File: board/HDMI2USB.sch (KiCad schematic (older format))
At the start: 0 parts

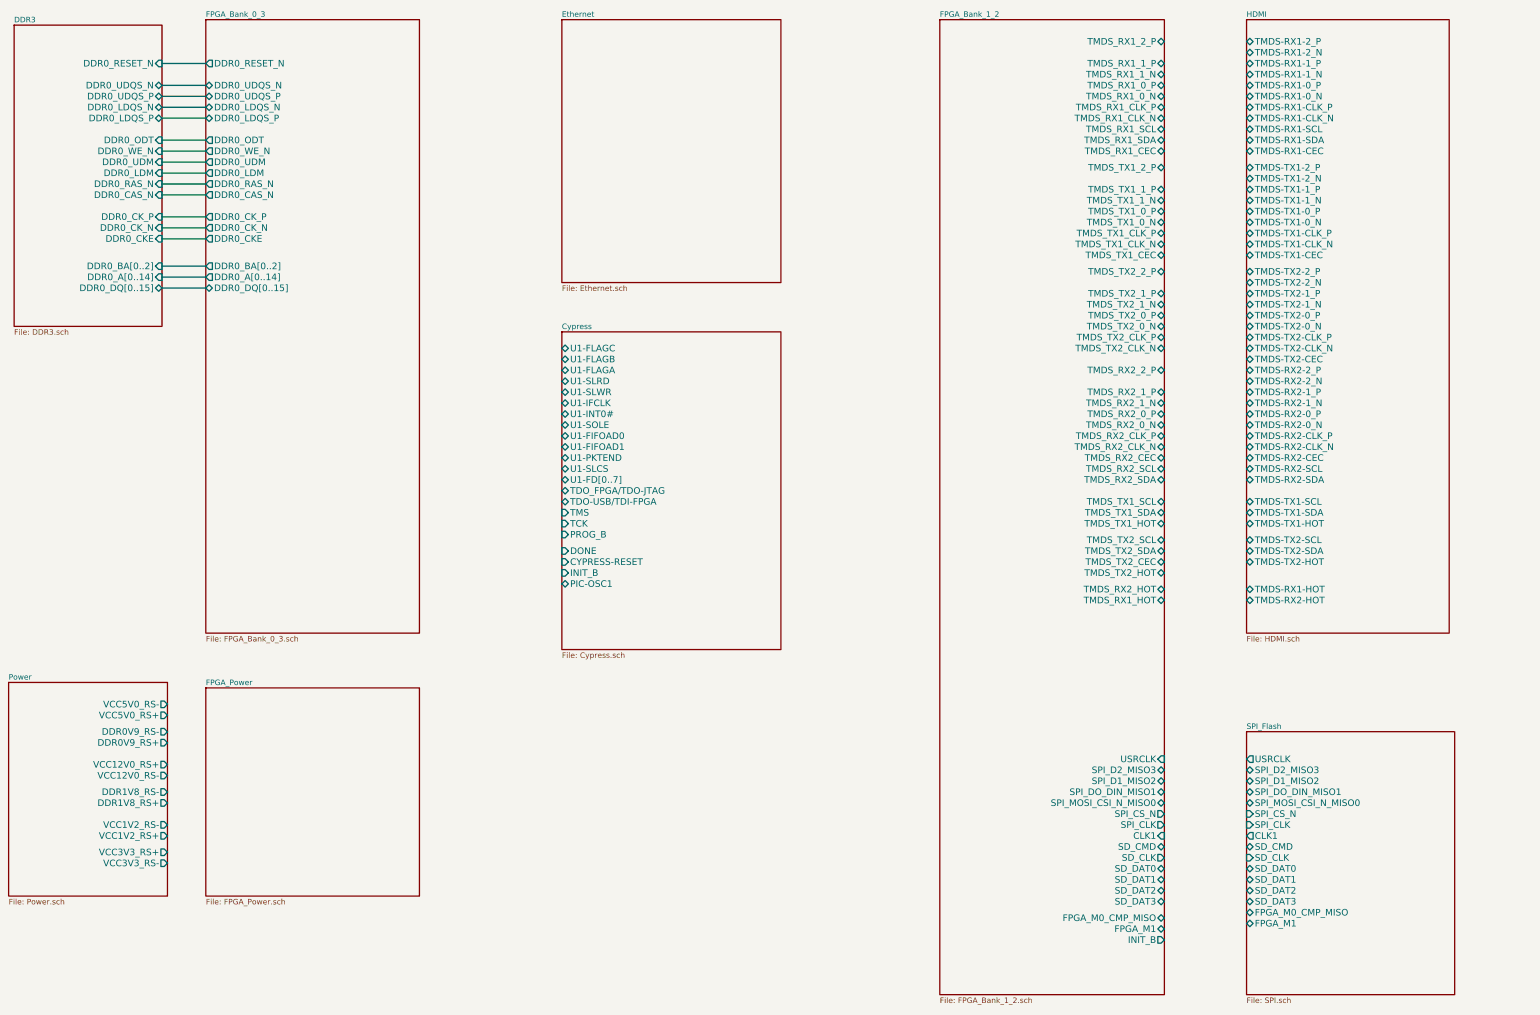
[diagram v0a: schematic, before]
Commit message: Issue #1458 - HDMI RX TX pins added, Cypress added, DDR added
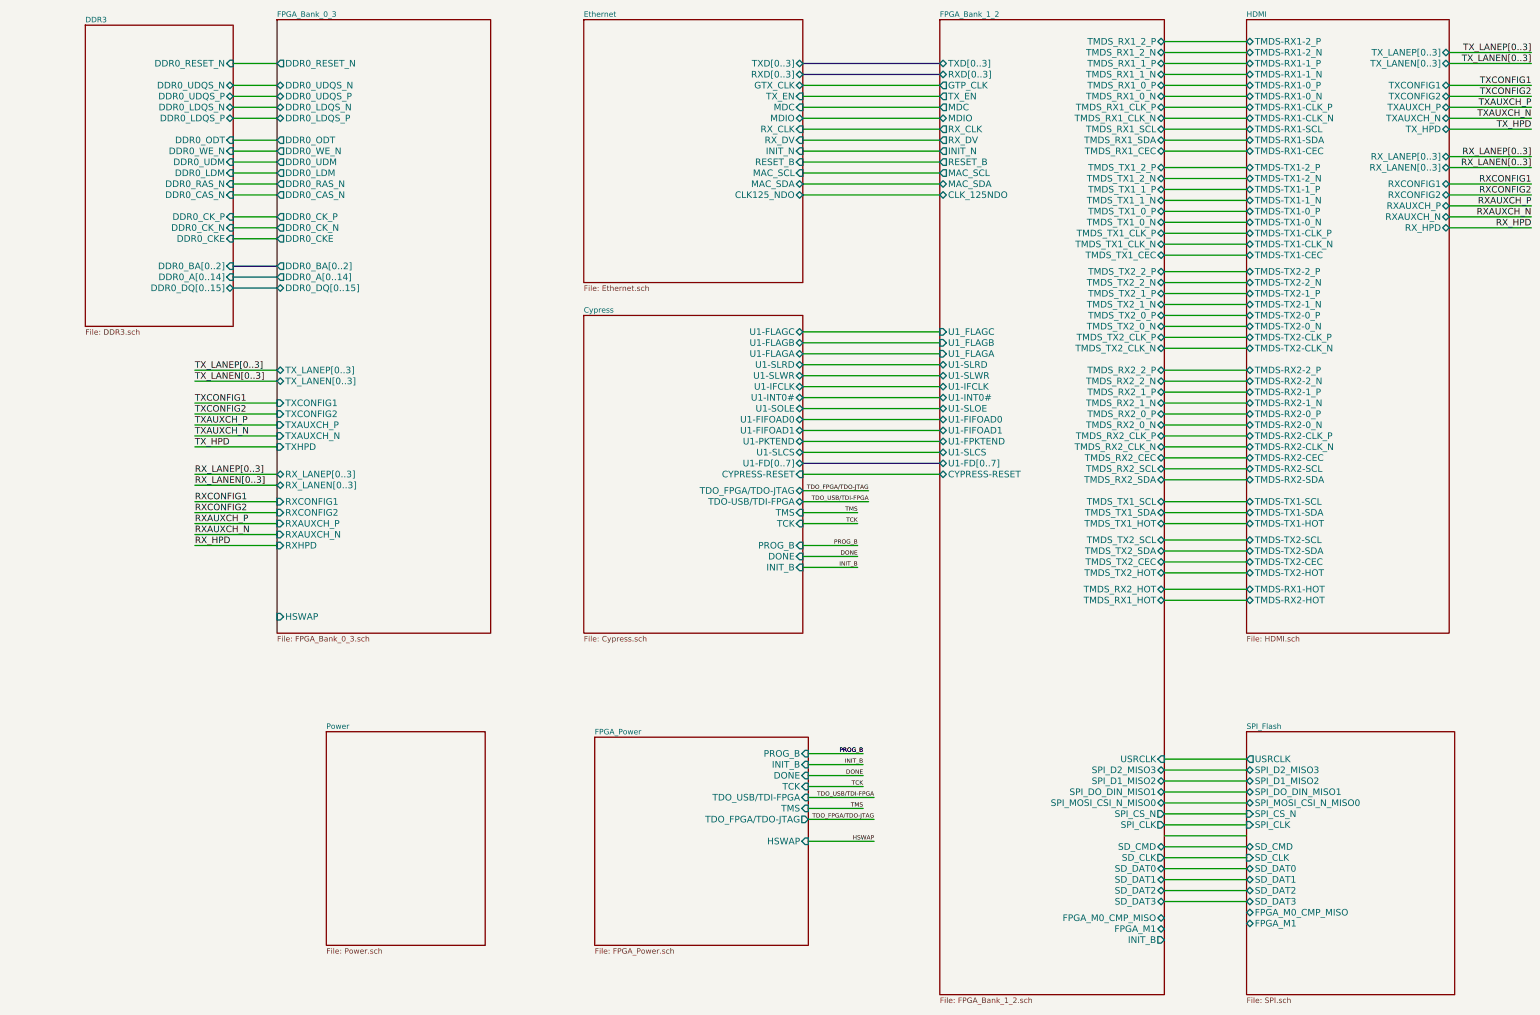
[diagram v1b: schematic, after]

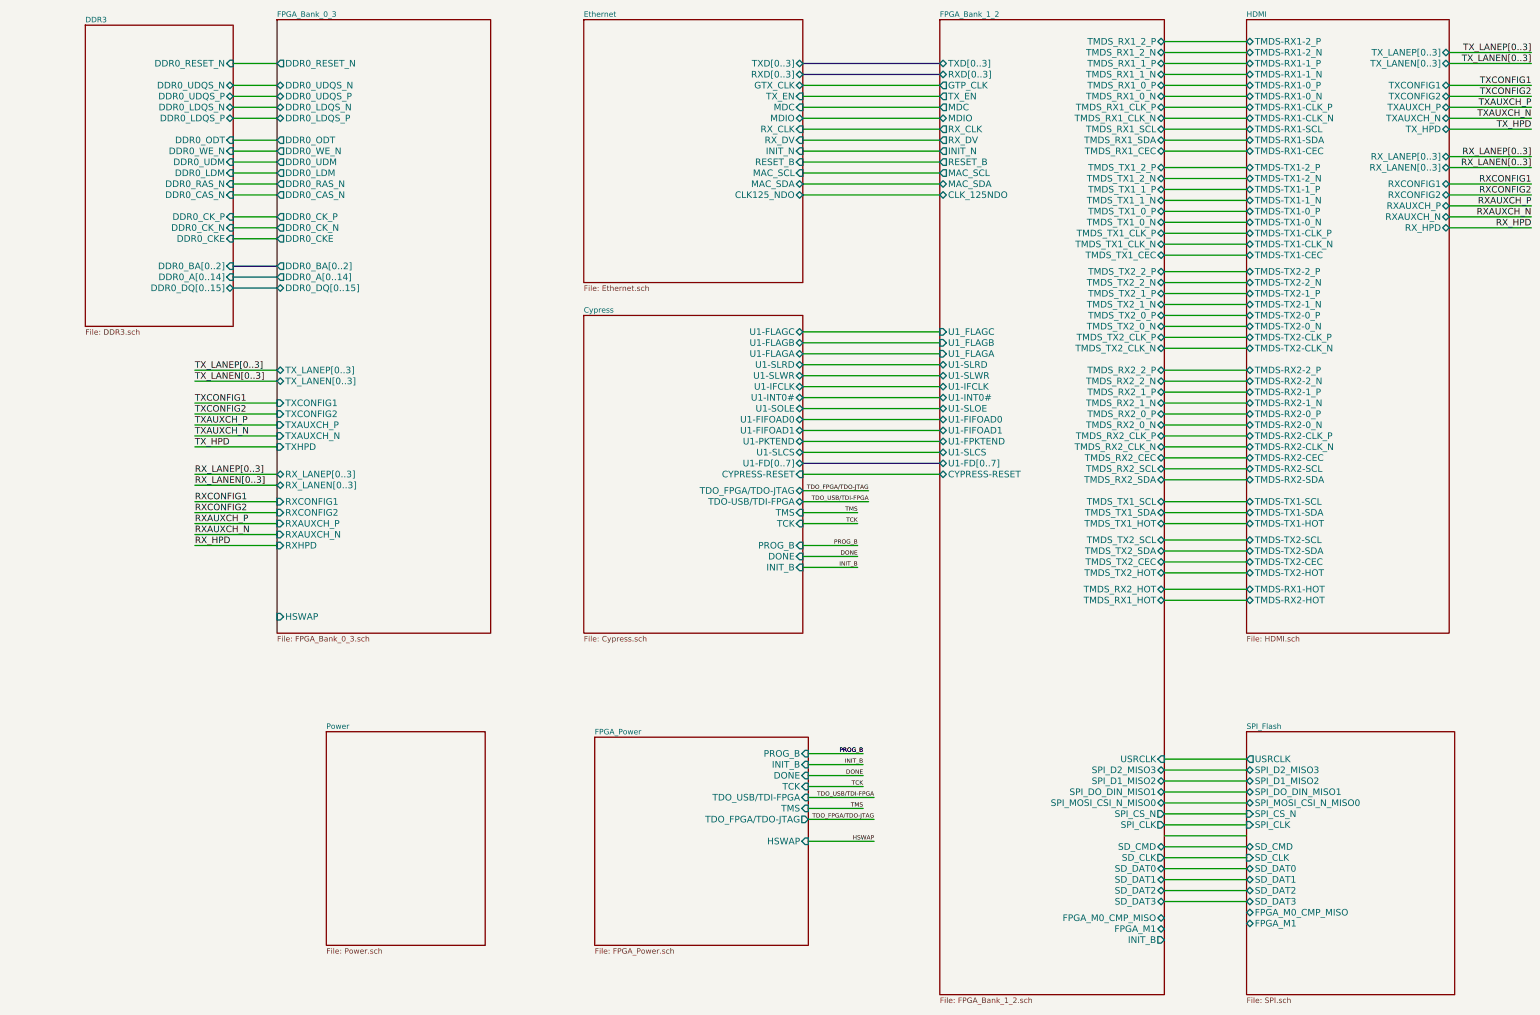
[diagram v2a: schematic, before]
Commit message: Issue #1470 - HDMI Sheet changes
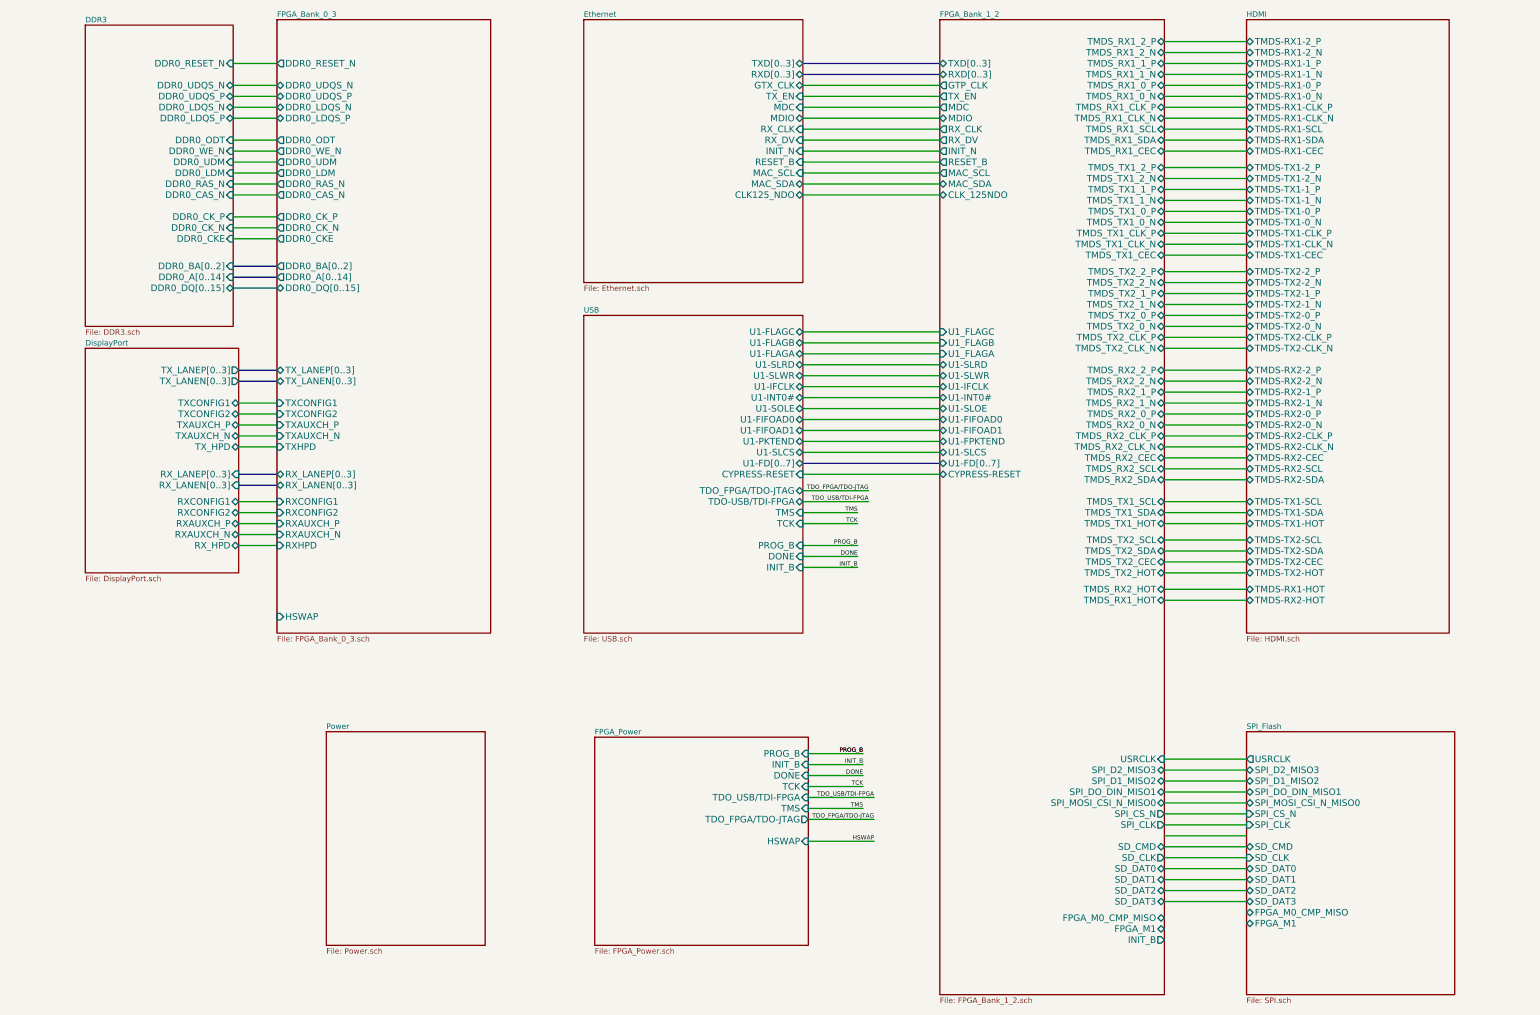
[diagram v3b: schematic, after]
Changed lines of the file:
@@
 LIBS:contrib
 LIBS:valves
-LIBS:hdmi2usb
 LIBS:HDMI2USB-cache
 EELAYER 27 0
@@
 $Descr A3 16535 11693
 encoding utf-8
-Sheet 1 10
+Sheet 1 11
 Title "HDMI2USB"
-Date "19 dec 2014"
+Date "29 dec 2014"
 Rev "Rev2"
 Comp ""
@@
 F32 "RXHPD" I L 3750 5900 60
 F33 "RXAUXCH_N" I L 3750 5800 60
-$EndSheet
-$Sheet
-S 12600 1100 1850 5600
-U 548A04AA
-F0 "HDMI" 50
-F1 "HDMI.sch" 50
-F2 "TMDS-RX1-2_P" B L 12600 1300 60
-F3 "TMDS-RX1-1_P" B L 12600 1500 60
-F4 "TMDS-RX1-0_P" B L 12600 1700 60
-F5 "TMDS-RX1-2_N" B L 12600 1400 60
-F6 "TMDS-RX1-1_N" B L 12600 1600 60
-F7 "TMDS-RX1-0_N" B L 12600 1800 60
-F8 "TMDS-RX1-CLK_P" B L 12600 1900 60
-F9 "TMDS-RX1-CLK_N" B L 12600 2000 60
-F10 "TMDS-RX1-SCL" B L 12600 2100 60
-F11 "TMDS-RX1-SDA" B L 12600 2200 60
-F12 "TMDS-TX1-2_P" B L 12600 2450 60
-F13 "TMDS-TX1-1_P" B L 12600 2650 60
-F14 "TMDS-TX1-0_P" B L 12600 2850 60
-F15 "TMDS-TX1-2_N" B L 12600 2550 60
-F16 "TMDS-TX1-1_N" B L 12600 2750 60
-F17 "TMDS-TX1-0_N" B L 12600 2950 60
-F18 "TMDS-TX1-CLK_P" B L 12600 3050 60
-F19 "TMDS-TX1-CLK_N" B L 12600 3150 60
-F20 "TMDS-TX2-2_P" B L 12600 3400 60
-F21 "TMDS-TX2-1_P" B L 12600 3600 60
-F22 "TMDS-TX2-0_P" B L 12600 3800 60
-F23 "TMDS-TX2-2_N" B L 12600 3500 60
-F24 "TMDS-TX2-1_N" B L 12600 3700 60
-F25 "TMDS-TX2-0_N" B L 12600 3900 60
-F26 "TMDS-TX2-CLK_P" B L 12600 4000 60
-F27 "TMDS-TX2-CLK_N" B L 12600 4100 60
-F28 "TMDS-RX2-2_P" B L 12600 4300 60
-F29 "TMDS-RX2-1_P" B L 12600 4500 60
-F30 "TMDS-RX2-0_P" B L 12600 4700 60
-F31 "TMDS-RX2-2_N" B L 12600 4400 60
-F32 "TMDS-RX2-1_N" B L 12600 4600 60
-F33 "TMDS-RX2-0_N" B L 12600 4800 60
-F34 "TMDS-RX2-CLK_P" B L 12600 4900 60
-F35 "TMDS-RX2-CLK_N" B L 12600 5000 60
-F36 "TMDS-TX1-CEC" B L 12600 3250 60
-F37 "TMDS-TX2-CEC" B L 12600 6050 60
-F38 "TMDS-RX1-CEC" B L 12600 2300 60
-F39 "TMDS-RX2-CEC" B L 12600 5100 60
-F40 "TMDS-RX2-SCL" B L 12600 5200 60
-F41 "TMDS-RX2-SDA" B L 12600 5300 60
-F42 "TMDS-TX1-SCL" B L 12600 5500 60
-F43 "TMDS-TX1-SDA" B L 12600 5600 60
-F44 "TMDS-TX1-HOT" B L 12600 5700 60
-F45 "TMDS-TX2-SCL" B L 12600 5850 60
-F46 "TMDS-TX2-SDA" B L 12600 5950 60
-F47 "TMDS-TX2-HOT" B L 12600 6150 60
-F48 "TMDS-RX1-HOT" B L 12600 6300 60
-F49 "TMDS-RX2-HOT" B L 12600 6400 60
-F50 "TX_LANEP[0..3]" B R 14450 1400 60
-F51 "TXCONFIG1" B R 14450 1700 60
-F52 "TXCONFIG2" B R 14450 1800 60
-F53 "TXAUXCH_P" B R 14450 1900 60
-F54 "TXAUXCH_N" B R 14450 2000 60
-F55 "RXCONFIG1" B R 14450 2600 60
-F56 "RXCONFIG2" B R 14450 2700 60
-F57 "RXAUXCH_P" B R 14450 2800 60
-F58 "RXAUXCH_N" B R 14450 2900 60
-F59 "TX_HPD" B R 14450 2100 60
-F60 "RX_HPD" B R 14450 3000 60
-F61 "TX_LANEN[0..3]" B R 14450 1500 60
-F62 "RX_LANEP[0..3]" B R 14450 2350 60
-F63 "RX_LANEN[0..3]" B R 14450 2450 60
 $EndSheet
 $Sheet
@@
 S 6550 3800 2000 2900
 U 54899593
-F0 "Cypress" 50
-F1 "Cypress.sch" 50
+F0 "USB" 50
+F1 "USB.sch" 50
 F2 "U1-FLAGC" B R 8550 3950 60
 F3 "U1-FLAGB" B R 8550 4050 60
@@
 Wire Bus Line
 	9800 5150 8550 5150
-Wire Wire Line
-	14450 1400 15200 1400
-Wire Wire Line
-	14450 1500 15200 1500
-Wire Wire Line
-	14450 1700 15200 1700
-Wire Wire Line
-	14450 1800 15200 1800
-Wire Wire Line
-	14450 1900 15200 1900
-Wire Wire Line
-	14450 2000 15200 2000
-Wire Wire Line
-	14450 2100 15200 2100
-Wire Wire Line
-	14450 2350 15200 2350
-Wire Wire Line
-	14450 2450 15200 2450
-Wire Wire Line
-	14450 2600 15200 2600
-Wire Wire Line
-	14450 2700 15200 2700
-Wire Wire Line
-	14450 2800 15200 2800
-Wire Wire Line
-	14450 2900 15200 2900
-Wire Wire Line
-	14450 3000 15200 3000
-Text Label 15200 1400 2    59   ~ 0
-TX_LANEP[0..3]
-Text Label 15200 1500 2    59   ~ 0
-TX_LANEN[0..3]
-Text Label 15200 1700 2    59   ~ 0
-TXCONFIG1
-Text Label 15200 1800 2    59   ~ 0
-TXCONFIG2
-Text Label 15200 1900 2    59   ~ 0
-TXAUXCH_P
-Text Label 15200 2000 2    59   ~ 0
-TXAUXCH_N
-Text Label 15200 2100 2    59   ~ 0
-TX_HPD
-Text Label 15200 2350 2    59   ~ 0
-RX_LANEP[0..3]
-Text Label 15200 2450 2    59   ~ 0
-RX_LANEN[0..3]
-Text Label 15200 2600 2    59   ~ 0
-RXCONFIG1
-Text Label 15200 2700 2    59   ~ 0
-RXCONFIG2
-Text Label 15200 2800 2    59   ~ 0
-RXAUXCH_P
-Text Label 15200 2900 2    59   ~ 0
-RXAUXCH_N
-Text Label 15200 3000 2    59   ~ 0
-RX_HPD
-Wire Wire Line
-	3750 4300 3000 4300
-Wire Wire Line
-	3750 4400 3000 4400
-Wire Wire Line
-	3750 4600 3000 4600
-Wire Wire Line
-	3750 4700 3000 4700
-Wire Wire Line
-	3750 4800 3000 4800
-Wire Wire Line
-	3750 4900 3000 4900
-Wire Wire Line
-	3750 5000 3000 5000
-Wire Wire Line
-	3750 5250 3000 5250
-Wire Wire Line
-	3750 5350 3000 5350
-Wire Wire Line
-	3750 5500 3000 5500
-Wire Wire Line
-	3750 5600 3000 5600
-Wire Wire Line
-	3750 5700 3000 5700
-Wire Wire Line
-	3750 5800 3000 5800
-Wire Wire Line
-	3750 5900 3000 5900
-Text Label 3000 4300 0    59   ~ 0
-TX_LANEP[0..3]
-Text Label 3000 4400 0    59   ~ 0
-TX_LANEN[0..3]
-Text Label 3000 4600 0    59   ~ 0
-TXCONFIG1
-Text Label 3000 4700 0    59   ~ 0
-TXCONFIG2
-Text Label 3000 4800 0    59   ~ 0
-TXAUXCH_P
-Text Label 3000 4900 0    59   ~ 0
-TXAUXCH_N
-Text Label 3000 5000 0    59   ~ 0
-TX_HPD
-Text Label 3000 5250 0    59   ~ 0
-RX_LANEP[0..3]
-Text Label 3000 5350 0    59   ~ 0
-RX_LANEN[0..3]
-Text Label 3000 5500 0    59   ~ 0
-RXCONFIG1
-Text Label 3000 5600 0    59   ~ 0
-RXCONFIG2
-Text Label 3000 5700 0    59   ~ 0
-RXAUXCH_P
-Text Label 3000 5800 0    59   ~ 0
-RXAUXCH_N
-Text Label 3000 5900 0    59   ~ 0
-RX_HPD
+$Sheet
+S 2000 4100 1400 2050
+U 54A2B817
+F0 "DisplayPort" 50
+F1 "DisplayPort.sch" 50
+F2 "TXCONFIG1" B R 3400 4600 60
+F3 "TXCONFIG2" B R 3400 4700 60
+F4 "RXCONFIG1" B R 3400 5500 60
+F5 "RXCONFIG2" B R 3400 5600 60
+F6 "TXAUXCH_P" B R 3400 4800 60
+F7 "TXAUXCH_N" B R 3400 4900 60
+F8 "RXAUXCH_P" B R 3400 5700 60
+F9 "RXAUXCH_N" B R 3400 5800 60
+F10 "TX_HPD" B R 3400 5000 60
+F11 "RX_HPD" B R 3400 5900 60
+F12 "RX_LANEP[0..3]" I R 3400 5250 60
+F13 "RX_LANEN[0..3]" I R 3400 5350 60
+F14 "TX_LANEP[0..3]" O R 3400 4300 60
+F15 "TX_LANEN[0..3]" O R 3400 4400 60
+$EndSheet
+Wire Bus Line
+	3400 4300 3750 4300
+Wire Bus Line
+	3400 4400 3750 4400
+Wire Bus Line
+	3400 5350 3750 5350
+Wire Bus Line
+	3400 5250 3750 5250
+Wire Wire Line
+	3400 5500 3750 5500
+Wire Wire Line
+	3400 5600 3750 5600
+Wire Wire Line
+	3400 5700 3750 5700
+Wire Wire Line
+	3400 5800 3750 5800
+Wire Wire Line
+	3400 5900 3750 5900
+Wire Wire Line
+	3400 5000 3750 5000
+Wire Wire Line
+	3400 4900 3750 4900
+Wire Wire Line
+	3400 4800 3750 4800
+Wire Wire Line
+	3400 4700 3750 4700
+Wire Wire Line
+	3400 4600 3750 4600
+$Sheet
+S 12600 1100 1850 5600
+U 548A04AA
+F0 "HDMI" 50
+F1 "HDMI.sch" 50
+F2 "TMDS-RX1-2_P" B L 12600 1300 60
+F3 "TMDS-RX1-1_P" B L 12600 1500 60
+F4 "TMDS-RX1-0_P" B L 12600 1700 60
+F5 "TMDS-RX1-2_N" B L 12600 1400 60
+F6 "TMDS-RX1-1_N" B L 12600 1600 60
+F7 "TMDS-RX1-0_N" B L 12600 1800 60
+F8 "TMDS-RX1-CLK_P" B L 12600 1900 60
+F9 "TMDS-RX1-CLK_N" B L 12600 2000 60
+F10 "TMDS-RX1-SCL" B L 12600 2100 60
+F11 "TMDS-RX1-SDA" B L 12600 2200 60
+F12 "TMDS-TX1-2_P" B L 12600 2450 60
+F13 "TMDS-TX1-1_P" B L 12600 2650 60
+F14 "TMDS-TX1-0_P" B L 12600 2850 60
+F15 "TMDS-TX1-2_N" B L 12600 2550 60
+F16 "TMDS-TX1-1_N" B L 12600 2750 60
+F17 "TMDS-TX1-0_N" B L 12600 2950 60
+F18 "TMDS-TX1-CLK_P" B L 12600 3050 60
+F19 "TMDS-TX1-CLK_N" B L 12600 3150 60
+F20 "TMDS-TX2-2_P" B L 12600 3400 60
+F21 "TMDS-TX2-1_P" B L 12600 3600 60
+F22 "TMDS-TX2-0_P" B L 12600 3800 60
+F23 "TMDS-TX2-2_N" B L 12600 3500 60
+F24 "TMDS-TX2-1_N" B L 12600 3700 60
+F25 "TMDS-TX2-0_N" B L 12600 3900 60
+F26 "TMDS-TX2-CLK_P" B L 12600 4000 60
+F27 "TMDS-TX2-CLK_N" B L 12600 4100 60
+F28 "TMDS-RX2-2_P" B L 12600 4300 60
+F29 "TMDS-RX2-1_P" B L 12600 4500 60
+F30 "TMDS-RX2-0_P" B L 12600 4700 60
+F31 "TMDS-RX2-2_N" B L 12600 4400 60
+F32 "TMDS-RX2-1_N" B L 12600 4600 60
+F33 "TMDS-RX2-0_N" B L 12600 4800 60
+F34 "TMDS-RX2-CLK_P" B L 12600 4900 60
+F35 "TMDS-RX2-CLK_N" B L 12600 5000 60
+F36 "TMDS-TX1-CEC" B L 12600 3250 60
+F37 "TMDS-TX2-CEC" B L 12600 6050 60
+F38 "TMDS-RX1-CEC" B L 12600 2300 60
+F39 "TMDS-RX2-CEC" B L 12600 5100 60
+F40 "TMDS-RX2-SCL" B L 12600 5200 60
+F41 "TMDS-RX2-SDA" B L 12600 5300 60
+F42 "TMDS-TX1-SCL" B L 12600 5500 60
+F43 "TMDS-TX1-SDA" B L 12600 5600 60
+F44 "TMDS-TX1-HOT" B L 12600 5700 60
+F45 "TMDS-TX2-SCL" B L 12600 5850 60
+F46 "TMDS-TX2-SDA" B L 12600 5950 60
+F47 "TMDS-TX2-HOT" B L 12600 6150 60
+F48 "TMDS-RX1-HOT" B L 12600 6300 60
+F49 "TMDS-RX2-HOT" B L 12600 6400 60
+$EndSheet
 $EndSCHEMATC
